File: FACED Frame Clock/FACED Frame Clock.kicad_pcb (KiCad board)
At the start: 2 copper layers, 100 x 100 mm, 42 parts, among them J2 Conn_Coaxial, J3 Conn_Coaxial, J4 Barrel_Jack_Switch, U1 LT1711xMS8, U2 TXU0202DCUR, U3 Teensy4.0

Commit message: move DC jack, more guard vias
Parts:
- moved J4 20.9 mm to (162.6, 171.1)
- moved C12 5.90 mm to (159.7, 143.4)
- moved C22 5.25 mm to (156.0, 144.7)
- moved C14 5.23 mm to (157.6, 144.7)
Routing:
- net Net-(C11-Pad1): track 3.18 -> 24.8 mm
- net Net-(PS1-+VIN): track 13.7 -> 5.68 mm
- net +5V: track 52.9 -> 58.8 mm
- net Net-(PS1-+VOUT): track 4.56 -> 3.77 mm
- net GND: track 20.4 -> 19.7 mm, vias 400 -> 426

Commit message: Revision submitted for order
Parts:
- added H5: MountingHole_Pad, MountingHole:MountingHole_2.2mm_M2_DIN965_Pad, F.Cu at (127.1, 113.3)
- added LOGO1: CC license, Custom Footprints:Creative_commons_license, F.Cu at (162.2, 83.2)
- added LOGO2: Jack Polarity, Custom Footprints:Polarity_Center_Positive, F.Cu at (163.1, 154.7)
- added LOGO3: OSHW Logo, Symbol:OSHW-Logo2_7.3x6mm_SilkScreen, F.Cu at (170.0, 85.9)
- moved C7 0.62 mm to (134.0, 109.7)
- moved C8 0.62 mm to (135.4, 109.7)
- turned C11 to -90 degrees
- turned C18 to 0 degrees
- turned C12 to 90 degrees
- turned C10 to 0 degrees
- turned C9 to 180 degrees
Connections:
- net Net-(PS1-+VOUT) renamed /9V
- C11 pad 1: Net-(C11-Pad1) -> +5V
- C11 pad 3: +5V -> Net-(C11-Pad3)
- C12 pad 1: +5V -> Net-(PS1-+VIN)
- C12 pad 3: Net-(PS1-+VIN) -> +5V
- C16 pad 2: Net-(PS1--VOUT) -> /-9V
- C18 pad 1: Net-(PS1--VOUT) -> Net-(LDO2-Vin)
- C18 pad 3: Net-(LDO2-Vin) -> /-9V
- J4 pad 1: Net-(C11-Pad1) -> Net-(C11-Pad3)
- J4 pad 3: unconnected-(J4-Pad3) -> GND
- PS1 pad 5: Net-(PS1--VOUT) -> /-9V
- U3 pad 11: unconnected-(U3-9_OUT1C-Pad11) -> /Frame_clock_3v3
- U3 pad 12: /Frame_clock_3v3 -> unconnected-(U3-10_CS_MQSR-Pad12)
- U3 pad 13: unconnected-(U3-11_MOSI_CTX1-Pad13) -> /Mirror_phase_3v3
- U3 pad 14: /Mirror_phase_3v3 -> unconnected-(U3-12_MISO_MQSL-Pad14)
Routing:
- net Net-(C11-Pad3): track 0.00 -> 24.8 mm
- net Net-(C11-Pad1): track 24.8 -> 0.00 mm
- net Net-(PS1--VOUT): track 15.2 -> 0.00 mm
- net /-9V: track 0.00 -> 15.2 mm
- net /Mirror_phase_3v3: track 8.45 -> 5.89 mm
- net /Frame_clock_3v3: track 9.25 -> 7.22 mm
- net +3V3: track 49.4 -> 47.7 mm
- net +5V: track 58.8 -> 60.1 mm
- net GND: vias 426 -> 431
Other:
- board text added: "*"
- board text added: "5V DC"
- board text added: "FACED Frame Clock"
- board text added: "Frame Clock Output (5V TTL)"
- board text added: "License: Creative Commons Attribution-ShareAlike 4.0 https://github.com/Llamero/FACED_Comparator_Frame_Clock Designed by: Benjamin E. Smith, Funded by: NIH P30EY003176"
- board text added: "Y-mirror Input (±6V Max)"

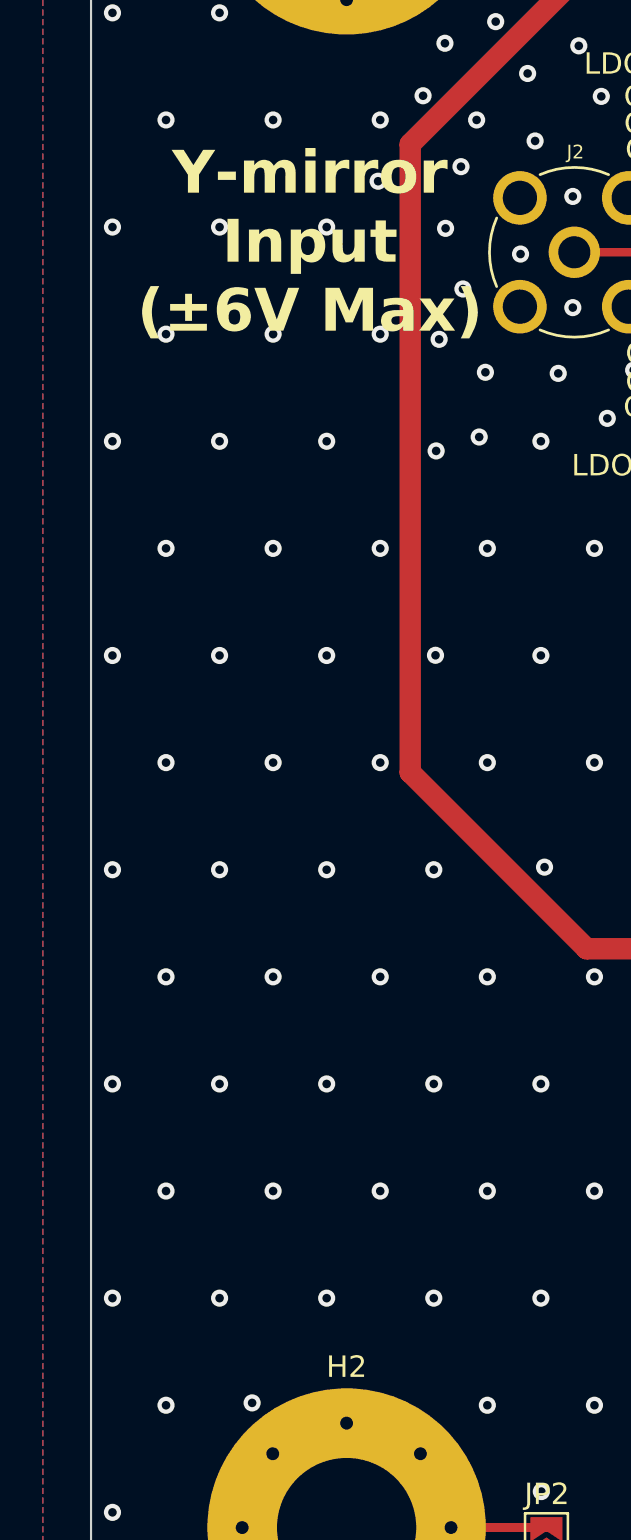
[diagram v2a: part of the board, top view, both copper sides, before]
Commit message: Improve grounding - thermal relief on mounting hole jumpers
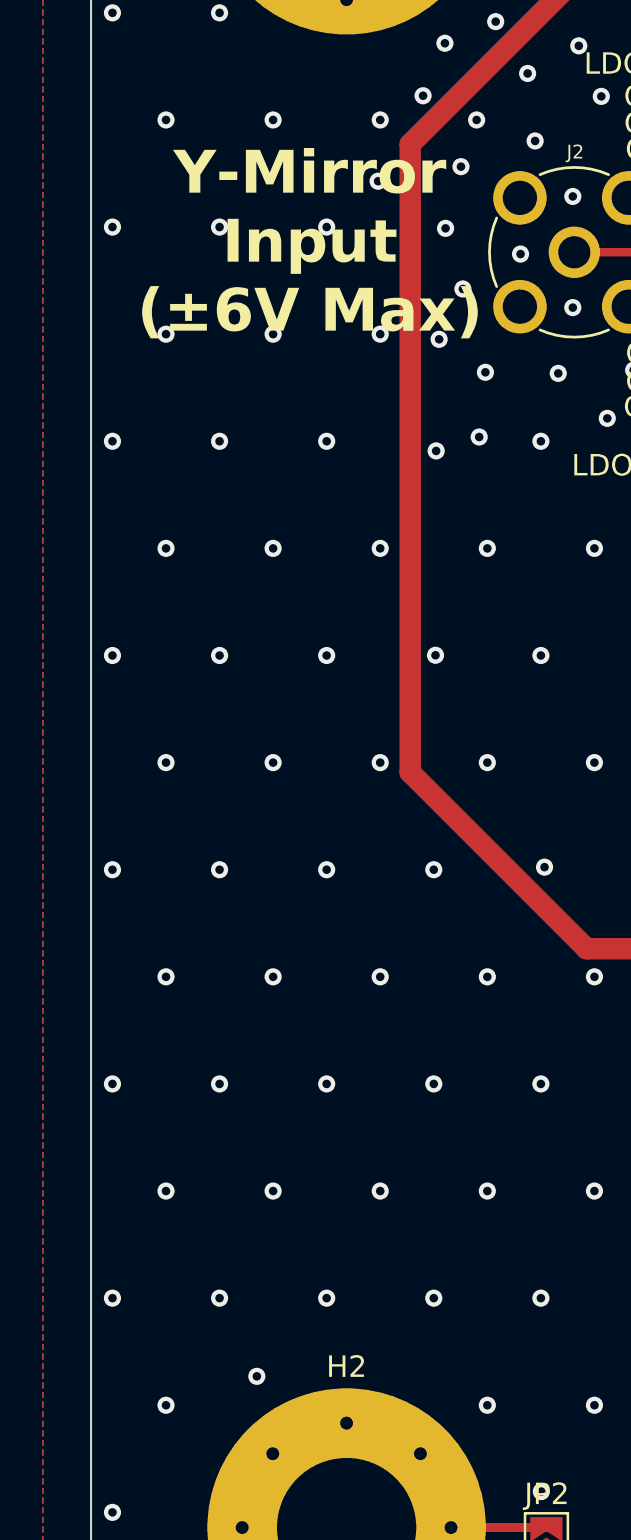
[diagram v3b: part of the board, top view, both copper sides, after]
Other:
- board text added: "Y-Mirror Input (±6V Max)"
- board text removed: "Y-mirror Input (±6V Max)"
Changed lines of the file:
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@@
       (stroke (width 0.05) (type solid)) (layer "F.CrtYd"))
     (pad "1" smd custom (at -0.725 0 90) (size 0.3 0.3) (layers "F.Cu" "F.Mask")
-      (net 1 "GND") (pinfunction "A") (pintype "passive") (zone_connect 2) (thermal_bridge_angle 45)
+      (net 1 "GND") (pinfunction "A") (pintype "passive") (zone_connect 1) (thermal_bridge_angle 45)
       (options (clearance outline) (anchor rect))
       (primitives
@@
       (stroke (width 0.05) (type solid)) (layer "F.CrtYd"))
     (pad "1" smd custom (at -0.725 0 90) (size 0.3 0.3) (layers "F.Cu" "F.Mask")
-      (net 1 "GND") (pinfunction "A") (pintype "passive") (zone_connect 2) (thermal_bridge_angle 45)
+      (net 1 "GND") (pinfunction "A") (pintype "passive") (zone_connect 1) (thermal_bridge_angle 45)
       (options (clearance outline) (anchor rect))
       (primitives
@@
     (property "ki_description" "Mounting Hole with connection")
     (property "ki_keywords" "mounting hole")
+    (zone_connect 2)
     (attr exclude_from_pos_files)
     (fp_text reference "H5" (at 0.39 3.04) (layer "F.SilkS")
@@
       (stroke (width 0.05) (type solid)) (layer "F.CrtYd"))
     (pad "1" smd custom (at -0.725 0 90) (size 0.3 0.3) (layers "F.Cu" "F.Mask")
-      (net 1 "GND") (pinfunction "A") (pintype "passive") (zone_connect 2) (thermal_bridge_angle 45)
+      (net 1 "GND") (pinfunction "A") (pintype "passive") (zone_connect 1) (thermal_bridge_angle 45)
       (options (clearance outline) (anchor rect))
       (primitives
@@
       (stroke (width 0.05) (type solid)) (layer "F.CrtYd"))
     (pad "1" smd custom (at -0.725 0 90) (size 0.3 0.3) (layers "F.Cu" "F.Mask")
-      (net 1 "GND") (pinfunction "A") (pintype "passive") (zone_connect 2) (thermal_bridge_angle 45)
+      (net 1 "GND") (pinfunction "A") (pintype "passive") (zone_connect 1) (thermal_bridge_angle 45)
       (options (clearance outline) (anchor rect))
       (primitives
@@
     (effects (font (size 1 1) (thickness 0.15)) (justify left))
   )
-  (gr_text "Y-mirror\nInput\n(±6V Max)" (at 105.22 112.58) (layer "F.SilkS")
+  (gr_text "Y-Mirror\nInput\n(±6V Max)" (at 105.22 112.58) (layer "F.SilkS")
     (effects (font (size 2 2) (thickness 0.2) bold) (justify bottom))
   )
@@
   (via (at 121 147.5) (size 0.8) (drill 0.4) (layers "F.Cu" "B.Cu") (free) (net 1))
   (via (at 133.5 82.5) (size 0.8) (drill 0.4) (layers "F.Cu" "B.Cu") (free) (net 1))
-  (via (at 102.52 162.39) (size 0.8) (drill 0.4) (layers "F.Cu" "B.Cu") (free) (net 1))
+  (via (at 102.74 161.15) (size 0.8) (drill 0.4) (layers "F.Cu" "B.Cu") (free) (net 1))
   (via (at 136 127.5) (size 0.8) (drill 0.4) (layers "F.Cu" "B.Cu") (free) (net 1))
   (via (at 163.5 92.5) (size 0.8) (drill 0.4) (layers "F.Cu" "B.Cu") (free) (net 1))
